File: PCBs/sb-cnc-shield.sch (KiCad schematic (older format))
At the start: 62 parts, among them P1 XMOT, P2 YMOT, P3 ZMOT, P4 AMOT, P5 UART, P6 I2C, P7 ES_SETUP, P8 12V-36V, SW1 RESET, U1 ARDUINO_UNO_SHIELD, U2 X, U3 Y, U4 Z, U5 A

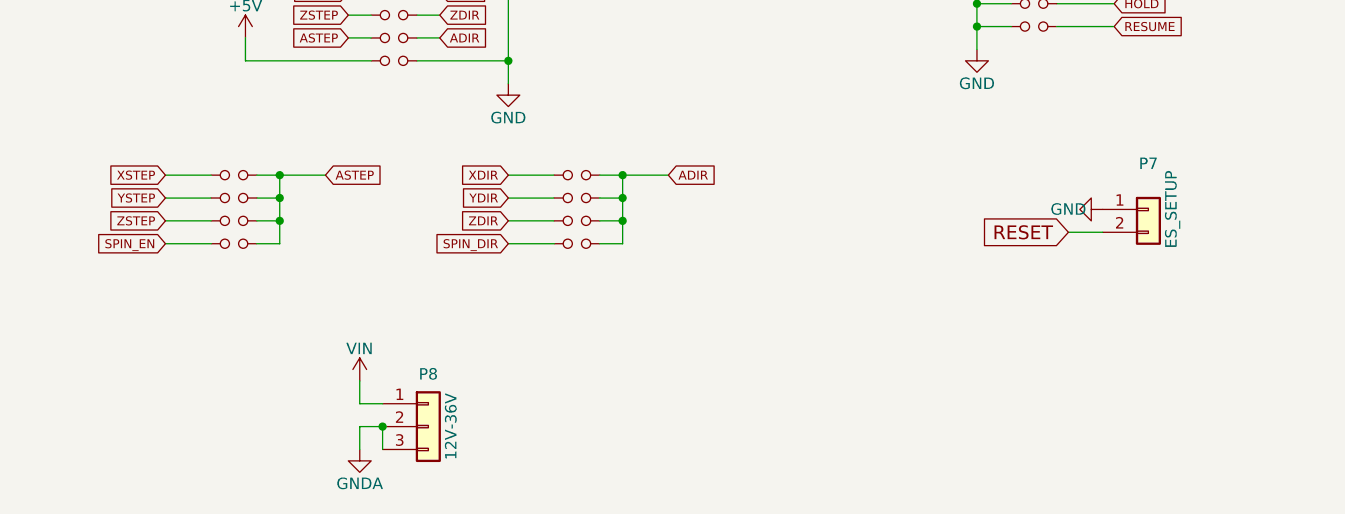
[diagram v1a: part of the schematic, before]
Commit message: add power button, lenghten pcb
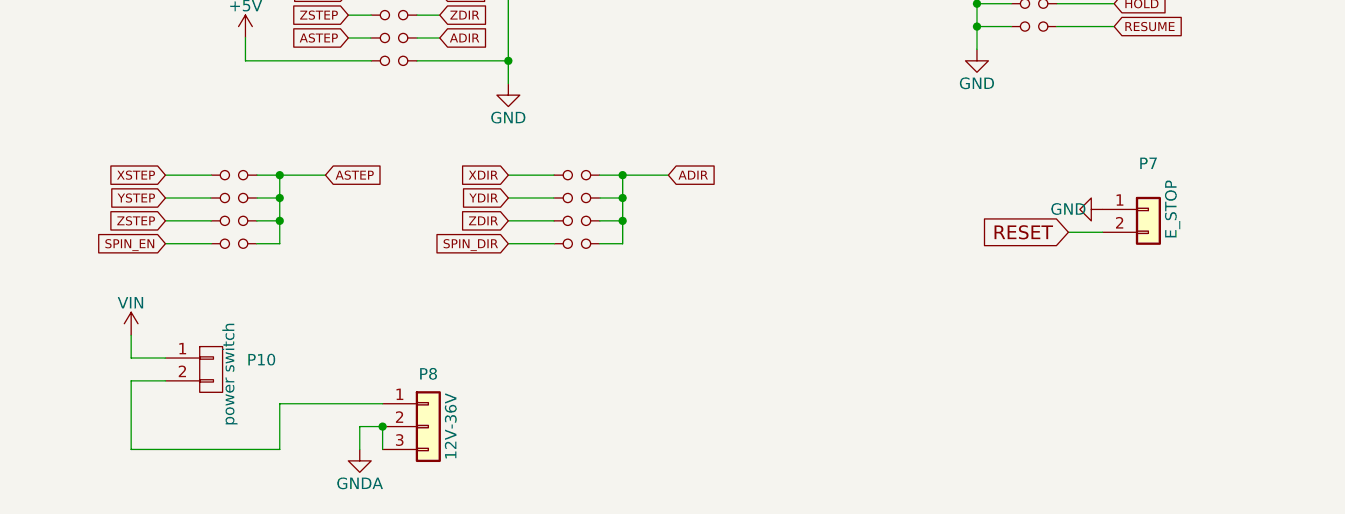
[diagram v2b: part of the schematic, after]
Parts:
- added P10: power switch, symbol sb-cnc-shield-rescue:CONN_01X02
- P7: value ES_SETUP -> E_STOP
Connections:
- net VIN: now also P10.1 (P1); no longer P8.1 (Pin_1)
- new net: P10.2 (P2), P8.1 (Pin_1)
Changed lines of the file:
@@
 L sb-cnc-shield-rescue:VIN #PWR038
 U 1 1 564DD2A8
-P 2400 6800
-F 0 "#PWR038" H 2400 6650 50  0001 C CNN
-F 1 "VIN" H 2400 6940 50  0000 C CNN
-F 2 "" H 2400 6800 60  0000 C CNN
-F 3 "" H 2400 6800 60  0000 C CNN
-	1    2400 6800
-	1    0    0    -1
-$EndComp
-Wire Wire Line
-	2500 6900 2400 6900
-Wire Wire Line
-	2400 6900 2400 6800
+P 1400 6600
+F 0 "#PWR038" H 1400 6450 50  0001 C CNN
+F 1 "VIN" H 1400 6740 50  0000 C CNN
+F 2 "" H 1400 6600 60  0000 C CNN
+F 3 "" H 1400 6600 60  0000 C CNN
+	1    1400 6600
+	1    0    0    -1
+$EndComp
+Wire Wire Line
+	1400 6700 1400 6600
 Wire Wire Line
 	2500 7000 2400 7000
@@
 P 5850 6050
 F 0 "P7" H 5850 6250 50  0000 C CNN
-F 1 "ES_SETUP" V 5950 6050 50  0000 C CNN
+F 1 "E_STOP" V 5950 6050 50  0000 C CNN
 F 2 "Connector_PinHeader_2.54mm:PinHeader_1x02_P2.54mm_Vertical" H 5850 6050 60  0001 C CNN
 F 3 "" H 5850 6050 60  0000 C CNN
@@
 Wire Wire Line
 	4700 3250 5100 3250
+$Comp
+L sb-cnc-shield-rescue:CONN_01X02 P10
+U 1 1 61767F9B
+P 1750 6750
+F 0 "P10" H 1906 6791 50  0000 L CNN
+F 1 "power switch" V 1828 6503 50  0000 L CNN
+F 2 "" H 1750 6750 50  0000 C CNN
+F 3 "" H 1750 6750 50  0000 C CNN
+	1    1750 6750
+	1    0    0    -1
+$EndComp
+Wire Wire Line
+	1400 6700 1550 6700
+Wire Wire Line
+	2500 6900 2050 6900
+Wire Wire Line
+	2050 6900 2050 7100
+Wire Wire Line
+	2050 7100 1400 7100
+Wire Wire Line
+	1400 7100 1400 6800
+Wire Wire Line
+	1400 6800 1550 6800
 $EndSCHEMATC

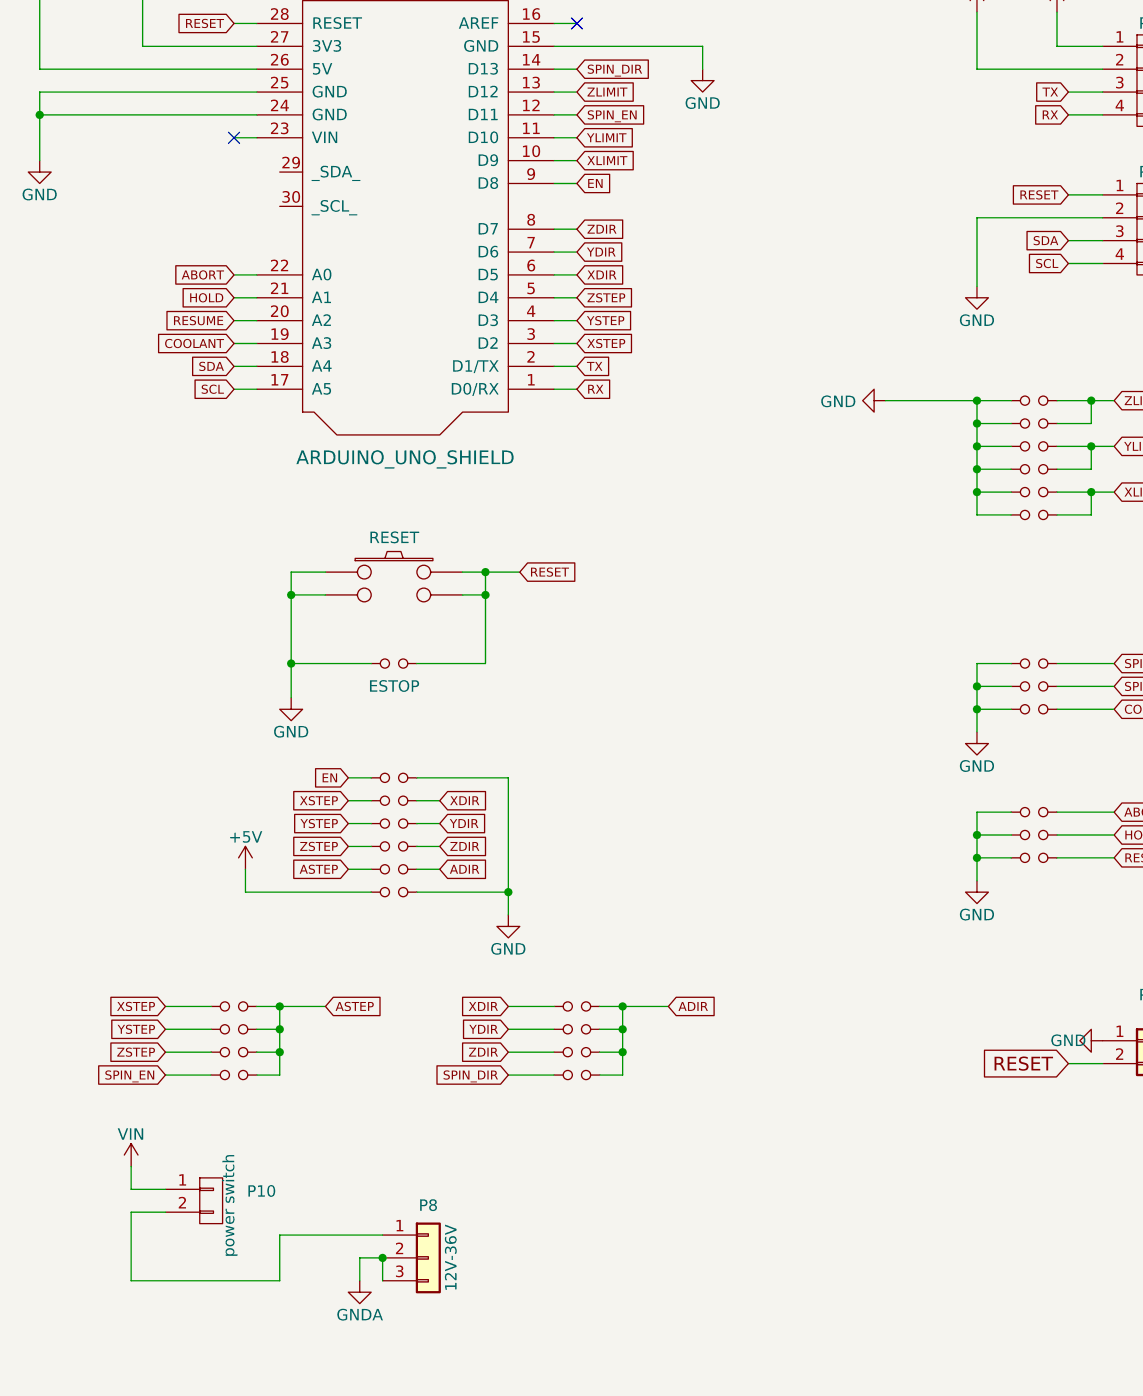
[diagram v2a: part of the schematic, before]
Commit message: add pump management circuit, I2C JST conn for display, JST power switch
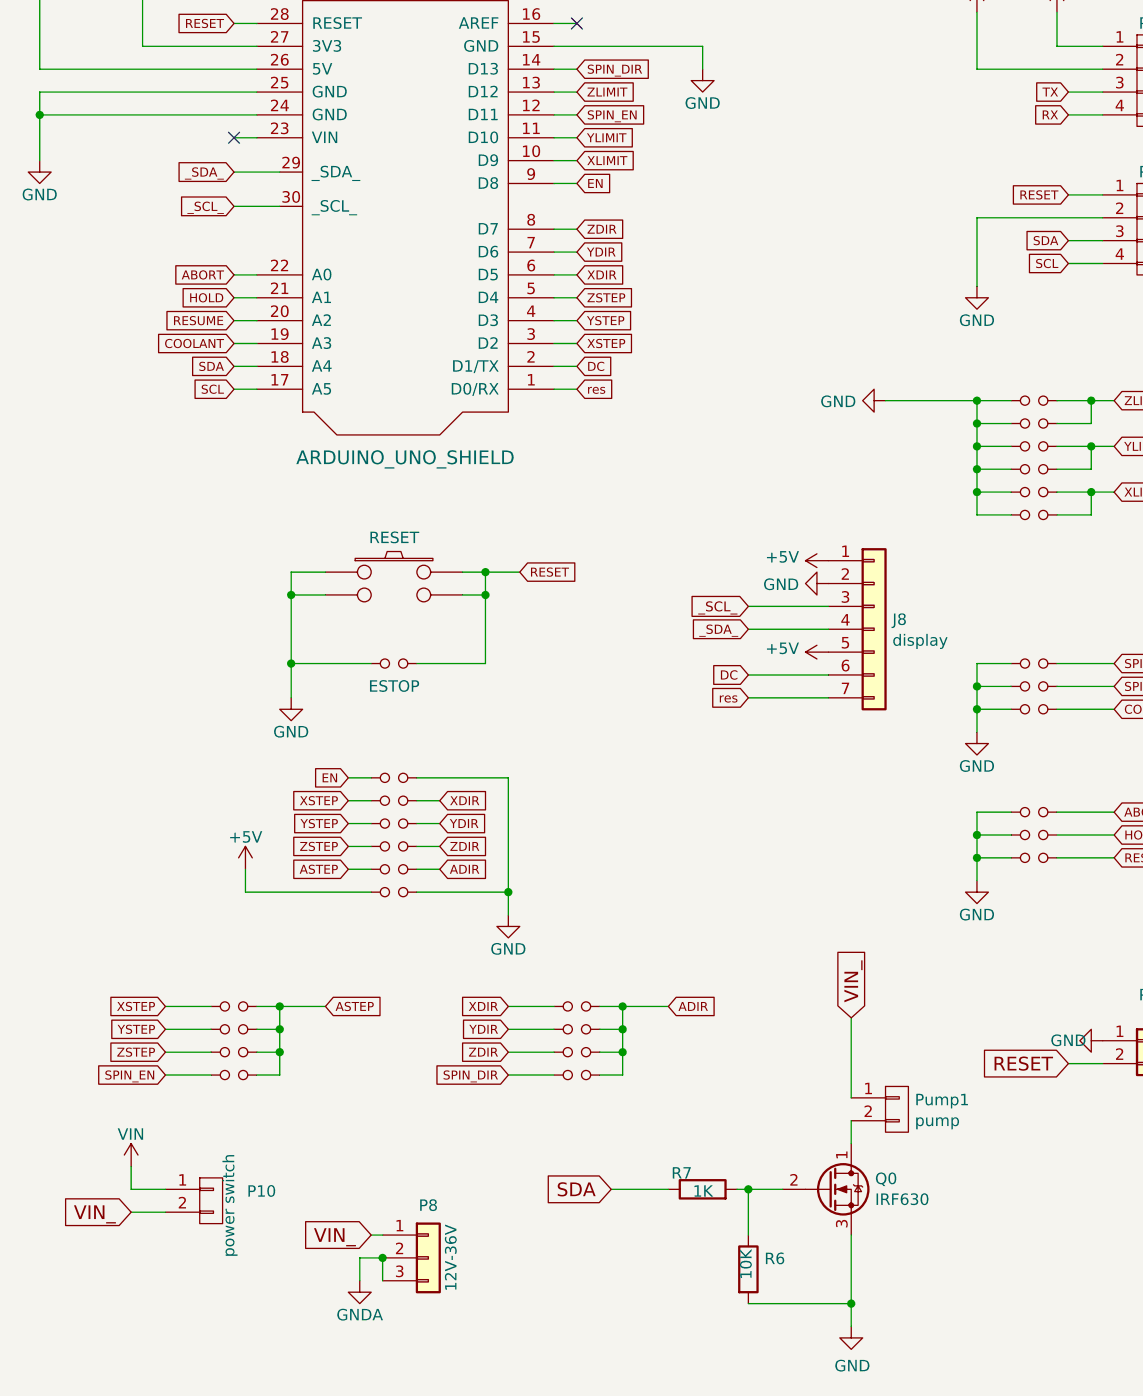
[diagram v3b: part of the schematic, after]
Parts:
- added J8: display, symbol Connector_Generic:Conn_01x07
- added Pump1: pump, Connector_PinHeader_2.54mm:PinHeader_1x02_P2.54mm_Vertical, symbol sb-cnc-shield-rescue:CONN_01X02
- added Q0: IRF630, Package_TO_SOT_THT:TO-220-3_Horizontal_TabDown, symbol Transistor_FET:IRF6631
- added R6: 10K, Resistor_SMD:R_0805_2012Metric, symbol Device:R
- added R7: 1K, Resistor_SMD:R_0805_2012Metric, symbol Device:R
- P10: footprint (none) -> Connector_PinHeader_2.54mm:PinHeader_1x02_P2.54mm_Vertical
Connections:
- net +5V: now also J8.1 (Pin_1), J8.5 (Pin_5)
- net GND: now also J8.2 (Pin_2), Q0.3 (S), R6.2
- net RX: no longer U1.1 (D0/RX)
- net SDA: now also R7.1
- net TX: no longer U1.2 (D1/TX)
- net _SDA_: now reaches U1.29 (_SDA_)
- net _SDA_: now also J8.4 (Pin_4)
- net _SCL_: now reaches U1.30 (_SCL_)
- net _SCL_: now also J8.3 (Pin_3)
- net VIN_: now reaches P10.2 (P2), P8.1 (Pin_1)
- net VIN_: now also Pump1.1 (P1)
- new net: Pump1.2 (P2), Q0.1 (D)
- new net: Q0.2 (G), R6.1, R7.2
- new net DC: J8.6 (Pin_6), U1.2 (D1/TX)
- new net res: J8.7 (Pin_7), U1.1 (D0/RX)
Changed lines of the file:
@@
 XSTEP
 Text GLabel 3350 3100 2    39   Input ~ 0
-TX
+DC
 Text GLabel 3350 3200 2    39   Input ~ 0
-RX
+res
 Wire Wire Line
 	3250 2500 3350 2500
@@
 F 0 "P10" H 1906 6791 50  0000 L CNN
 F 1 "power switch" V 1828 6503 50  0000 L CNN
-F 2 "" H 1750 6750 50  0000 C CNN
+F 2 "Connector_PinHeader_2.54mm:PinHeader_1x02_P2.54mm_Vertical" H 1750 6750 50  0001 C CNN
 F 3 "" H 1750 6750 50  0000 C CNN
 	1    1750 6750
@@
 Wire Wire Line
 	1400 6700 1550 6700
-Wire Wire Line
-	2500 6900 2050 6900
-Wire Wire Line
-	2050 6900 2050 7100
-Wire Wire Line
-	2050 7100 1400 7100
-Wire Wire Line
-	1400 7100 1400 6800
+Text GLabel 2450 6900 0    60   Input ~ 0
+VIN_
+Wire Wire Line
+	2450 6900 2500 6900
+Text GLabel 1400 6800 0    60   Input ~ 0
+VIN_
 Wire Wire Line
 	1400 6800 1550 6800
+$Comp
+L Transistor_FET:IRF6631 Q0
+U 1 1 61840DF5
+P 4450 6700
+F 0 "Q0" H 4654 6746 50  0000 L CNN
+F 1 "IRF630" H 4654 6655 50  0000 L CNN
+F 2 "Package_TO_SOT_THT:TO-220-3_Horizontal_TabDown" H 4450 6700 50  0001 C CIN
+F 3 "https://www.infineon.com/dgdl/irf6631pbf.pdf?fileId=5546d462533600a4015355e8d0561a37" H 4450 6700 50  0001 L CNN
+	1    4450 6700
+	1    0    0    -1
+$EndComp
+$Comp
+L power:GND #PWR0102
+U 1 1 6184791C
+P 4550 7300
+F 0 "#PWR0102" H 4550 7050 50  0001 C CNN
+F 1 "GND" H 4555 7127 50  0000 C CNN
+F 2 "" H 4550 7300 50  0001 C CNN
+F 3 "" H 4550 7300 50  0001 C CNN
+	1    4550 7300
+	1    0    0    -1
+$EndComp
+Wire Wire Line
+	4550 6900 4550 7200
+$Comp
+L sb-cnc-shield-rescue:CONN_01X02 Pump1
+U 1 1 6189F36F
+P 4750 6350
+F 0 "Pump1" H 4828 6391 50  0000 L CNN
+F 1 "pump" H 4828 6300 50  0000 L CNN
+F 2 "Connector_PinHeader_2.54mm:PinHeader_1x02_P2.54mm_Vertical" H 4750 6350 50  0001 C CNN
+F 3 "" H 4750 6350 50  0000 C CNN
+	1    4750 6350
+	1    0    0    -1
+$EndComp
+Wire Wire Line
+	4550 6500 4550 6400
+Text GLabel 4550 5950 1    60   Input ~ 0
+VIN_
+Wire Wire Line
+	4550 5950 4550 6300
+$Comp
+L Device:R R6
+U 1 1 61920A00
+P 4100 7050
+F 0 "R6" H 4170 7096 50  0000 L CNN
+F 1 "10K" V 4091 7005 50  0000 L CNN
+F 2 "Resistor_SMD:R_0805_2012Metric" V 4030 7050 50  0001 C CNN
+F 3 "~" H 4100 7050 50  0001 C CNN
+	1    4100 7050
+	1    0    0    -1
+$EndComp
+$Comp
+L Device:R R7
+U 1 1 61967CD3
+P 3900 6700
+F 0 "R7" V 3970 6746 50  0000 L CNN
+F 1 "1K" V 3891 6655 50  0000 L CNN
+F 2 "Resistor_SMD:R_0805_2012Metric" V 3830 6700 50  0001 C CNN
+F 3 "~" H 3900 6700 50  0001 C CNN
+	1    3900 6700
+	0    -1   -1   0
+$EndComp
+Wire Wire Line
+	4050 6700 4100 6700
+Wire Wire Line
+	4100 6900 4100 6700
+Connection ~ 4100 6700
+Wire Wire Line
+	4100 6700 4250 6700
+Wire Wire Line
+	4100 7200 4550 7200
+Connection ~ 4550 7200
+Wire Wire Line
+	4550 7200 4550 7300
+Text GLabel 3500 6700 0    60   Input ~ 0
+SDA
+Wire Wire Line
+	3500 6700 3750 6700
+$Comp
+L power:+5V #PWR?
+U 1 1 61B1D8D5
+P 4450 3950
+F 0 "#PWR?" H 4450 3800 50  0001 C CNN
+F 1 "+5V" V 4465 4078 50  0000 L CNN
+F 2 "" H 4450 3950 50  0001 C CNN
+F 3 "" H 4450 3950 50  0001 C CNN
+	1    4450 3950
+	0    -1   -1   0
+$EndComp
+$Comp
+L power:GND #PWR?
+U 1 1 61B1E602
+P 4450 4050
+F 0 "#PWR?" H 4450 3800 50  0001 C CNN
+F 1 "GND" V 4455 3922 50  0000 R CNN
+F 2 "" H 4450 4050 50  0001 C CNN
+F 3 "" H 4450 4050 50  0001 C CNN
+	1    4450 4050
+	0    1    1    0
+$EndComp
+Text GLabel 4100 4150 0    43   Input ~ 0
+_SCL_
+Wire Wire Line
+	4450 4150 4100 4150
+Text GLabel 1850 2250 0    40   Input ~ 0
+_SDA_
+Text GLabel 1850 2400 0    40   Input ~ 0
+_SCL_
+Wire Wire Line
+	1850 2250 2050 2250
+Wire Wire Line
+	2050 2400 1850 2400
+Text GLabel 4100 4250 0    40   Input ~ 0
+_SDA_
+Wire Wire Line
+	4100 4250 4450 4250
+$Comp
+L power:+5V #PWR?
+U 1 1 61BA3AF7
+P 4450 4350
+F 0 "#PWR?" H 4450 4200 50  0001 C CNN
+F 1 "+5V" V 4465 4478 50  0000 L CNN
+F 2 "" H 4450 4350 50  0001 C CNN
+F 3 "" H 4450 4350 50  0001 C CNN
+	1    4450 4350
+	0    -1   -1   0
+$EndComp
+Text GLabel 4100 4450 0    40   Input ~ 0
+DC
+Wire Wire Line
+	4450 4450 4100 4450
+$Comp
+L Connector_Generic:Conn_01x07 J8
+U 1 1 61BC4556
+P 4650 4250
+F 0 "J8" H 4730 4292 50  0000 L CNN
+F 1 "display" H 4730 4201 50  0000 L CNN
+F 2 "" H 4650 4250 50  0001 C CNN
+F 3 "~" H 4650 4250 50  0001 C CNN
+	1    4650 4250
+	1    0    0    -1
+$EndComp
+Text GLabel 4100 4550 0    40   Input ~ 0
+res
+Wire Wire Line
+	4100 4550 4450 4550
 $EndSCHEMATC
